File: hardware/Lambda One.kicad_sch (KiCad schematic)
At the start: 7 parts, among them IC1 01, SW1 SW_Push, U1 W65C816SxP, U2 28C256, U3 ATF22V10C, U4 AS6C1008-xxP, U5 74HC74

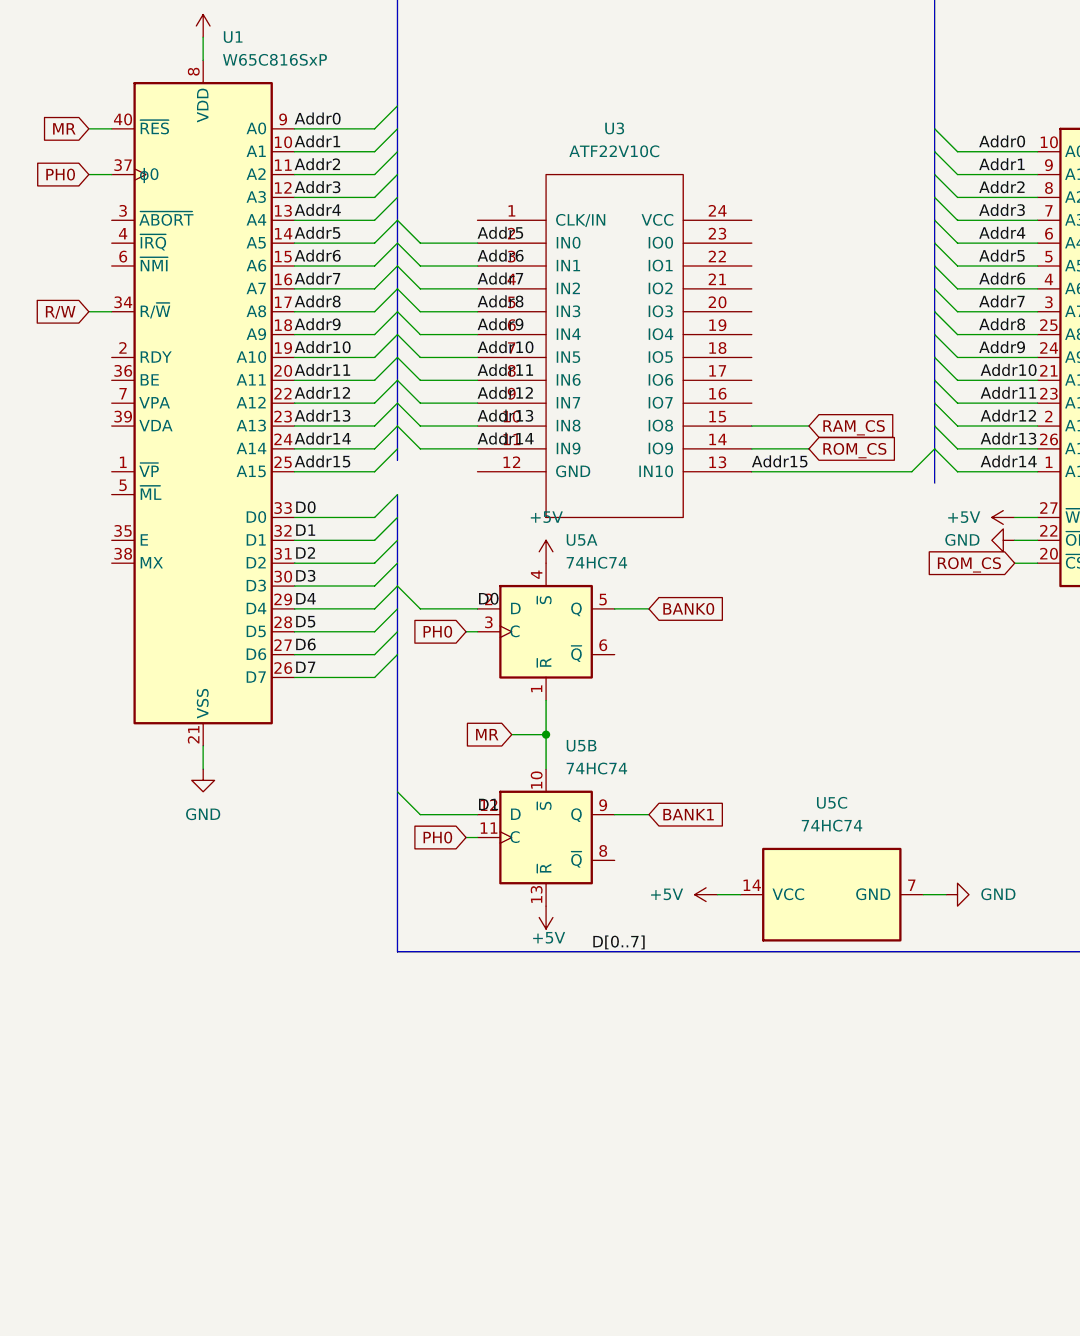
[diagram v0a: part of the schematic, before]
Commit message: Fixed mem banking
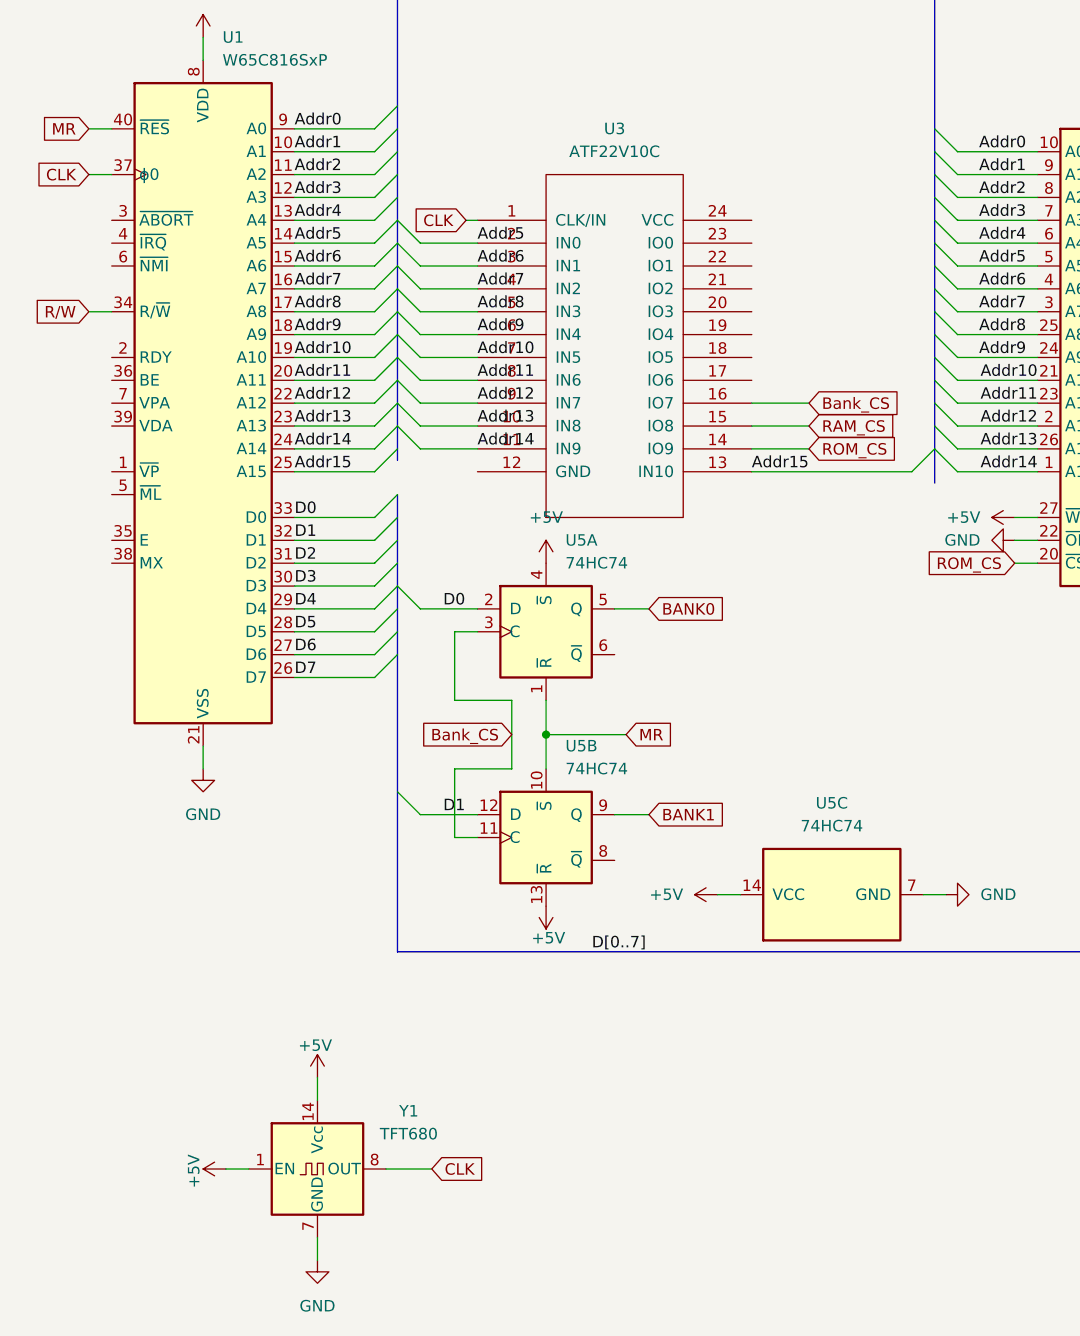
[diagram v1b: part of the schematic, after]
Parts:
- added Y1: TFT680, Oscillator:Oscillator_DIP-14, symbol Oscillator:TFT680
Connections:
- net +5V: now also Y1.1 (EN), Y1.14 (Vcc)
- net GND: now also Y1.7 (GND)
- net CLK: now reaches U3.1 (CLK/IN)
- net CLK: now also U1.37 (ϕ0), Y1.8 (OUT)
- net Bank_CS: now reaches U3.16 (IO7)
- net Bank_CS: now also U5.11 (C), U5.3 (C)
- removed net PH0: U1.37 (ϕ0), U5.11 (C), U5.3 (C)

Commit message: Modularized
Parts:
- removed U2: 28C256, symbol Memory_EEPROM:28C256
- removed U4: AS6C1008-xxP, Package_DIP:DIP-32_W15.24mm, symbol Memory_RAM:AS6C1008-xxP
- removed U5: 74HC74, symbol 74xx:74HC74
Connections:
- net GND: now also U3.12 (GND)
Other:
- added sheet Memory Sheet (mem.kicad_sch)
- moved on the sheet: IC1, SW1, U1, U3, Y1

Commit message: Added gpio
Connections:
- net GPIO_CS: now reaches U3.17 (IO6)
- net R/W renamed R/~{W}
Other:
- added sheet GPIO (gpio.kicad_sch)
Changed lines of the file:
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@@
+	(wire
+		(pts
+			(xy 175.26 87.63) (xy 181.61 87.63)
+		)
+		(stroke
+			(width 0)
+			(type default)
+		)
+	)
 	(wire
 		(pts
@@
 		)
 	)
-	(global_label "R{slash}W"
-		(shape input)
-		(at 88.9 80.01 180)
-		(fields_autoplaced yes)
-		(effects
-			(font
-				(size 1.27 1.27)
-			)
-			(justify right)
-		)
-		(property "Intersheetrefs" "${INTERSHEET_REFS}"
-			(at 81.8629 80.01 0)
-			(effects
-				(font
-					(size 1.27 1.27)
-				)
-				(justify right)
-				(hide yes)
-			)
-		)
-	)
 	(global_label "CLK"
 		(shape input)
@@
 	)
 	(global_label "ROM_CS"
-		(shape input)
+		(shape output)
 		(at 181.61 95.25 0)
 		(fields_autoplaced yes)
@@
 	)
 	(global_label "D[0..7]"
-		(shape input)
+		(shape bidirectional)
 		(at 151.13 151.13 0)
 		(fields_autoplaced yes)
@@
 		)
 		(property "Intersheetrefs" "${INTERSHEET_REFS}"
-			(at 160.7072 151.13 0)
+			(at 161.8185 151.13 0)
 			(effects
 				(font
@@
 	)
 	(global_label "Bank_CS"
-		(shape input)
+		(shape output)
 		(at 181.61 90.17 0)
 		(fields_autoplaced yes)
@@
 		)
 	)
+	(global_label "R{slash}~{W}"
+		(shape output)
+		(at 88.9 80.01 180)
+		(fields_autoplaced yes)
+		(effects
+			(font
+				(size 1.27 1.27)
+			)
+			(justify right)
+		)
+		(property "Intersheetrefs" "${INTERSHEET_REFS}"
+			(at 81.8629 80.01 0)
+			(effects
+				(font
+					(size 1.27 1.27)
+				)
+				(justify right)
+				(hide yes)
+			)
+		)
+	)
 	(global_label "Addr[0..15]"
-		(shape input)
+		(shape output)
 		(at 199.39 29.21 0)
 		(fields_autoplaced yes)
@@
 	)
 	(global_label "RAM_CS"
-		(shape input)
+		(shape output)
 		(at 181.61 92.71 0)
 		(fields_autoplaced yes)
@@
 		(property "Intersheetrefs" "${INTERSHEET_REFS}"
 			(at 191.8523 92.71 0)
+			(effects
+				(font
+					(size 1.27 1.27)
+				)
+				(justify left)
+				(hide yes)
+			)
+		)
+	)
+	(global_label "GPIO_CS"
+		(shape output)
+		(at 181.61 87.63 0)
+		(fields_autoplaced yes)
+		(effects
+			(font
+				(size 1.27 1.27)
+			)
+			(justify left)
+		)
+		(property "Intersheetrefs" "${INTERSHEET_REFS}"
+			(at 192.5176 87.63 0)
 			(effects
 				(font
@@
 				)
 			)
+		)
+	)
+	(sheet
+		(at 247.65 138.43)
+		(size 34.29 8.89)
+		(exclude_from_sim no)
+		(in_bom yes)
+		(on_board yes)
+		(dnp no)
+		(fields_autoplaced yes)
+		(stroke
+			(width 0.1524)
+			(type solid)
+		)
+		(fill
+			(color 0 0 0 0.0000)
+		)
+		(property "Sheetname" "GPIO"
+			(at 247.65 137.7184 0)
+			(effects
+				(font
+					(size 1.27 1.27)
+				)
+				(justify left bottom)
+			)
+		)
+		(property "Sheetfile" "gpio.kicad_sch"
+			(at 247.65 147.9046 0)
+			(effects
+				(font
+					(size 1.27 1.27)
+				)
+				(justify left top)
+			)
+		)
+		(instances
+			(project "Lambda One"
+				(path "/73ea9964-373f-4fdc-b03e-f532cf836c0d"
+					(page "3")
+				)
+			)

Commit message: Improved labels
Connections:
- net Bank_CS renamed BANK_{CS}
- net GPIO_CS renamed GPIO_{CS}
- net RAM_CS renamed RAM_{~{CS}}
- net ROM_CS renamed ROM_{~{CS}}
- no-connect marks 0 -> 7
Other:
- moved on the sheet: Y1
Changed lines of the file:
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@@
 		(color 0 0 0 0)
+	)
+	(no_connect
+		(at 175.26 69.85)
+	)
+	(no_connect
+		(at 175.26 72.39)
+	)
+	(no_connect
+		(at 175.26 77.47)
+	)
+	(no_connect
+		(at 175.26 82.55)
+	)
+	(no_connect
+		(at 175.26 85.09)
+	)
+	(no_connect
+		(at 175.26 80.01)
+	)
+	(no_connect
+		(at 175.26 74.93)
 	)
 	(bus_entry
@@
 	(wire
 		(pts
-			(xy 38.1 184.15) (xy 38.1 186.69)
+			(xy 246.38 55.88) (xy 246.38 58.42)
 		)
 		(stroke
@@
 	(wire
 		(pts
-			(xy 27.94 176.53) (xy 30.48 176.53)
+			(xy 236.22 48.26) (xy 238.76 48.26)
 		)
 		(stroke
@@
 	(wire
 		(pts
-			(xy 38.1 166.37) (xy 38.1 168.91)
+			(xy 246.38 38.1) (xy 246.38 40.64)
 		)
 		(stroke
@@
 	(wire
 		(pts
-			(xy 45.72 176.53) (xy 50.8 176.53)
+			(xy 254 48.26) (xy 259.08 48.26)
 		)
 		(stroke
@@
 	(global_label "CLK"
 		(shape input)
-		(at 50.8 176.53 0)
+		(at 259.08 48.26 0)
 		(fields_autoplaced yes)
 		(effects
@@
 		)
 		(property "Intersheetrefs" "${INTERSHEET_REFS}"
-			(at 57.3533 176.53 0)
+			(at 265.6333 48.26 0)
 			(effects
 				(font
@@
 		)
 	)
-	(global_label "ROM_CS"
+	(global_label "ROM_{~{CS}}"
 		(shape output)
 		(at 181.61 95.25 0)
@@
 		)
 		(property "Intersheetrefs" "${INTERSHEET_REFS}"
-			(at 192.0942 95.25 0)
+			(at 190.6815 95.25 0)
 			(effects
 				(font
@@
 		)
 	)
-	(global_label "Bank_CS"
+	(global_label "BANK_{CS}"
 		(shape output)
 		(at 181.61 90.17 0)
@@
 		)
 		(property "Intersheetrefs" "${INTERSHEET_REFS}"
-			(at 192.6384 90.17 0)
+			(at 191.5887 90.17 0)
 			(effects
 				(font
@@
 		)
 	)
-	(global_label "RAM_CS"
+	(global_label "RAM_{~{CS}}"
 		(shape output)
 		(at 181.61 92.71 0)
@@
 		)
 		(property "Intersheetrefs" "${INTERSHEET_REFS}"
-			(at 191.8523 92.71 0)
+			(at 190.4396 92.71 0)
 			(effects
 				(font
@@
 		)
 	)
-	(global_label "GPIO_CS"
+	(global_label "GPIO_{CS}"
 		(shape output)
 		(at 181.61 87.63 0)
@@
 		)
 		(property "Intersheetrefs" "${INTERSHEET_REFS}"
-			(at 192.5176 87.63 0)
+			(at 191.1049 87.63 0)
 			(effects
 				(font
@@
 	(symbol
 		(lib_id "power:+5V")
-		(at 27.94 176.53 90)
+		(at 236.22 48.26 90)
 		(unit 1)
 		(exclude_from_sim no)
@@
 		(dnp no)
 		(property "Reference" "#PWR020"
-			(at 31.75 176.53 0)
+			(at 240.03 48.26 0)
 			(effects
 				(font
@@
 		)
 		(property "Value" "+5V"
-			(at 24.384 176.784 0)
+			(at 232.664 48.514 0)
 			(effects
 				(font
@@
 		)
 		(property "Footprint" ""
-			(at 27.94 176.53 0)
+			(at 236.22 48.26 0)
 			(effects
 				(font
@@
 		)
 		(property "Datasheet" ""
-			(at 27.94 176.53 0)
+			(at 236.22 48.26 0)
 			(effects
 				(font
@@
 		)
 		(property "Description" "Power symbol creates a global label with name \"+5V\""
-			(at 27.94 176.53 0)
+			(at 236.22 48.26 0)
 			(effects
 				(font
@@
 	(symbol
 		(lib_id "power:+5V")
-		(at 38.1 166.37 0)
+		(at 246.38 38.1 0)
 		(unit 1)
 		(exclude_from_sim no)
@@
 		(dnp no)
 		(property "Reference" "#PWR014"
-			(at 38.1 170.18 0)
+			(at 246.38 41.91 0)
 			(effects
 				(font
@@
 		)
 		(property "Value" "+5V"
-			(at 38.1 162.306 0)
+			(at 246.38 34.036 0)
 			(effects
 				(font
@@
 		)
 		(property "Footprint" ""
-			(at 38.1 166.37 0)
+			(at 246.38 38.1 0)
 			(effects
 				(font
@@
 		)
 		(property "Datasheet" ""
-			(at 38.1 166.37 0)
+			(at 246.38 38.1 0)
 			(effects
 				(font
@@
 		)
 		(property "Description" "Power symbol creates a global label with name \"+5V\""
-			(at 38.1 166.37 0)
+			(at 246.38 38.1 0)
 			(effects
 				(font
@@
 	(symbol
 		(lib_id "Oscillator:TFT680")
-		(at 38.1 176.53 0)
+		(at 246.38 48.26 0)
 		(unit 1)
 		(exclude_from_sim no)
@@
 		(fields_autoplaced yes)
 		(property "Reference" "Y1"
-			(at 48.26 170.1098 0)
+			(at 256.54 41.8398 0)
 			(effects
 				(font
@@
 		)
 		(property "Value" "TFT680"
-			(at 48.26 172.6498 0)
+			(at 256.54 44.3798 0)
 			(effects
 				(font
@@
 		)
 		(property "Footprint" "Oscillator:Oscillator_DIP-14"
-			(at 49.53 185.42 0)
+			(at 257.81 57.15 0)
 			(effects
 				(font
@@
 		)
 		(property "Datasheet" "http://cdn-reichelt.de/documents/datenblatt/B400/OSZI.pdf"
-			(at 35.56 176.53 0)
+			(at 243.84 48.26 0)
 			(effects
 				(font
@@
 		)
 		(property "Description" "Crystal Clock Oscillator, DIP14-style metal package"
-			(at 38.1 176.53 0)
+			(at 246.38 48.26 0)
 			(effects
 				(font
@@
 	(symbol
 		(lib_id "power:GND")
-		(at 38.1 186.69 0)
+		(at 246.38 58.42 0)
 		(unit 1)
 		(exclude_from_sim no)
@@
 		(fields_autoplaced yes)
 		(property "Reference" "#PWR019"
-			(at 38.1 193.04 0)
+			(at 246.38 64.77 0)
 			(effects
 				(font
@@
 		)
 		(property "Value" "GND"
-			(at 38.1 191.77 0)
+			(at 246.38 63.5 0)
 			(effects
 				(font
@@
 		)
 		(property "Footprint" ""
-			(at 38.1 186.69 0)
+			(at 246.38 58.42 0)
 			(effects
 				(font
@@
 		)
 		(property "Datasheet" ""
-			(at 38.1 186.69 0)
+			(at 246.38 58.42 0)
 			(effects
 				(font
@@
 		)
 		(property "Description" "Power symbol creates a global label with name \"GND\" , ground"
-			(at 38.1 186.69 0)
-			(effects
-				(font
+			(at 246.38 58.42 0)
+			(effects
+				(font

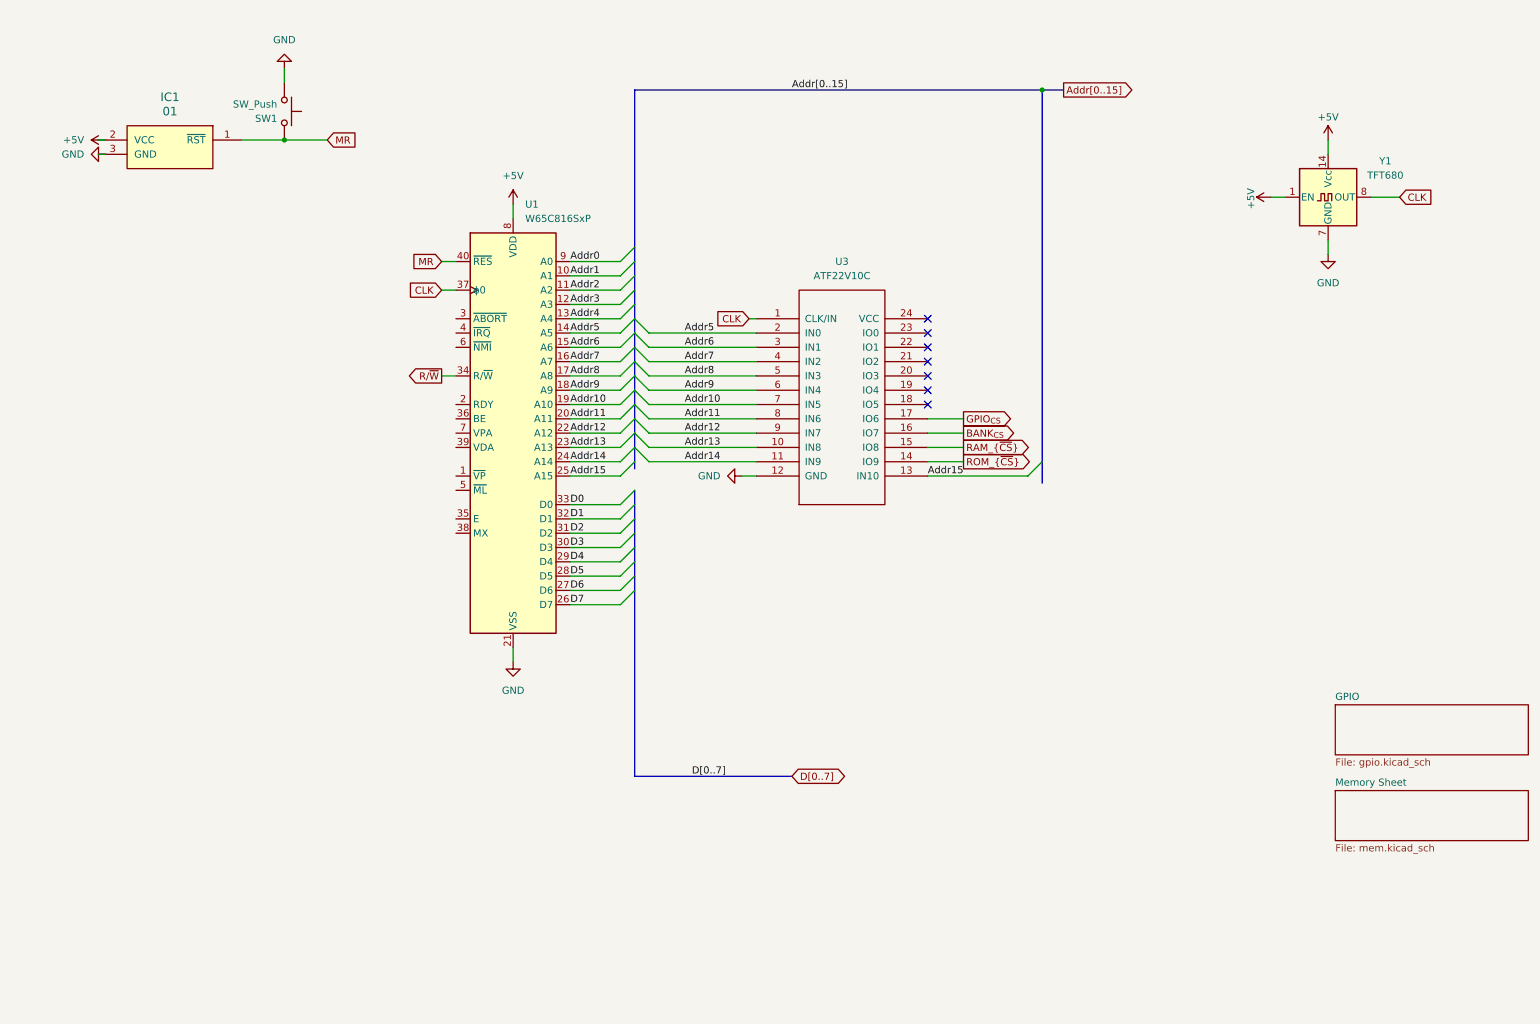
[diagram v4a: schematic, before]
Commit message: Improved Schematics and added fooprints
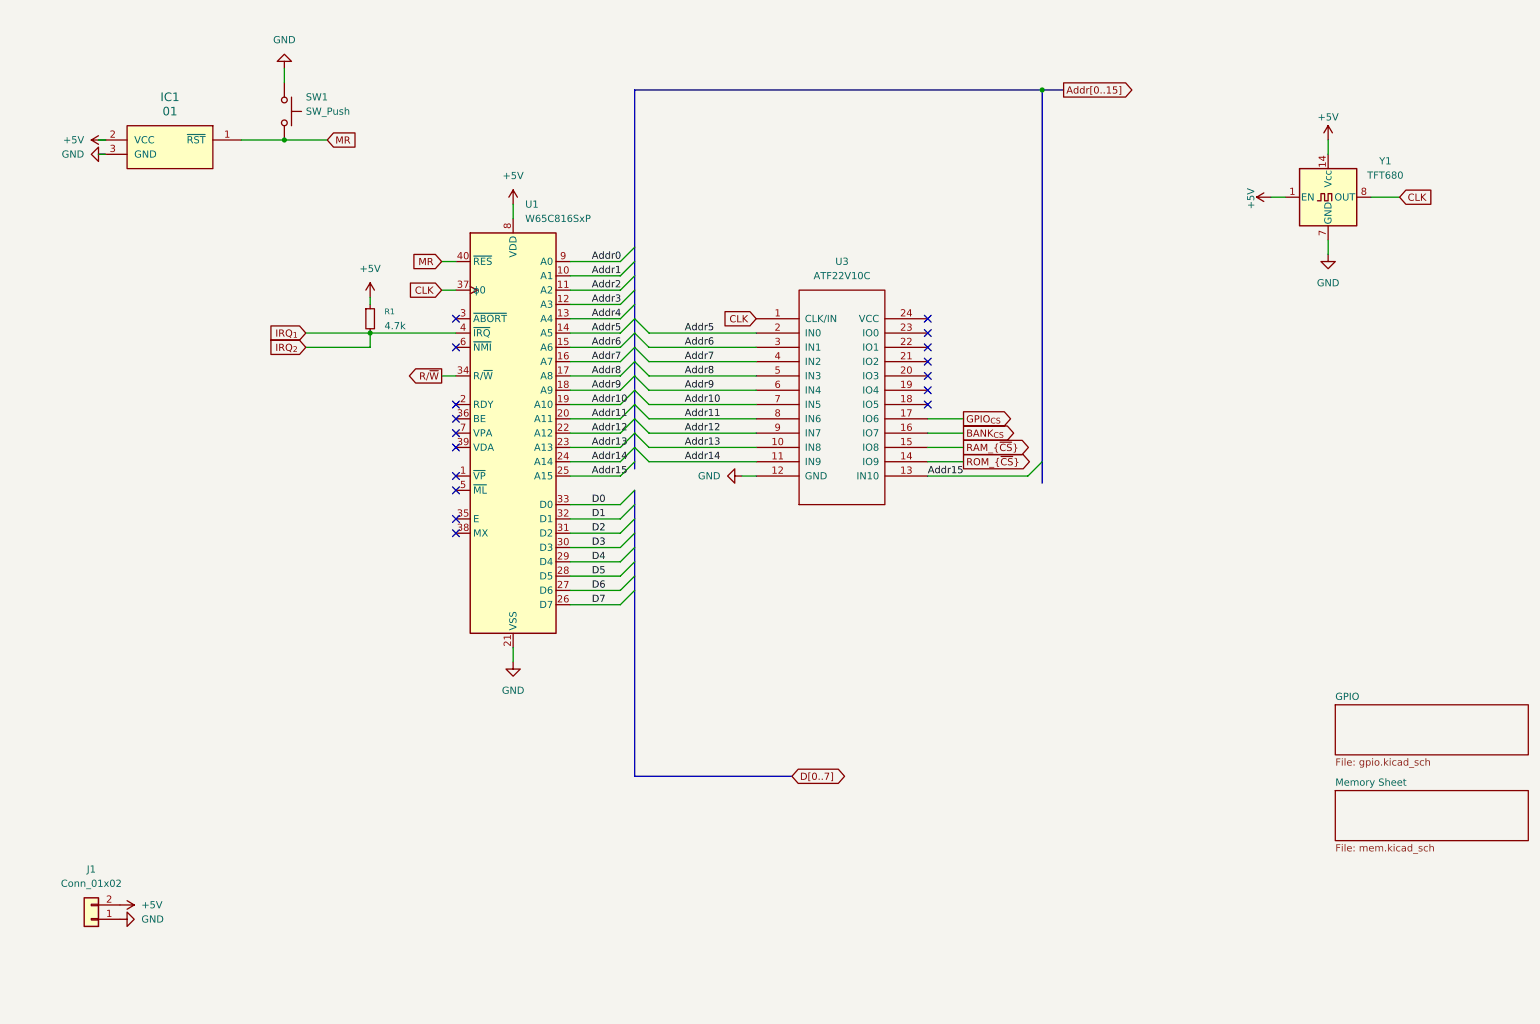
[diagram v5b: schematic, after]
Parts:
- added J1: Conn_01x02, Connector_JST:JST_XH_B2B-XH-A_1x02_P2.50mm_Vertical, symbol Connector_Generic:Conn_01x02
- added R1: 4.7k, symbol Device:R_Small
- IC1: footprint (none) -> DS1813-5:TO92127P495H695-3
- SW1: footprint (none) -> Button_Switch_SMD:SW_Push_1P1T_NO_CK_PTS125Sx73PSMTR
- U3: footprint MODULE -> ATF22V10C-10PU:24-DIP
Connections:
- net +5V: now also J1.2 (Pin_2), R1.1
- net GND: now also J1.1 (Pin_1)
- net IRQ_{1}: now reaches U1.4 (~{IRQ})
- net IRQ_{1}: now also R1.2
- no-connect marks 7 -> 17

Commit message: Added Clock and Ethernet via SPI
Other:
- added sheet Internal SPI (spi.kicad_sch)
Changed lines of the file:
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@@
 		(rev "v1")
 		(company "Embrace")
+		(comment 1 "https://github.com/Apoll011/Lambda-One")
+		(comment 2 "Apoll011")
+		(comment 3 "Draw by Tiago Inês")
 	)
 	(junction
@@
 				)
 			)
+		)
+	)
+	(sheet
+		(at 247.65 119.38)
+		(size 34.29 13.97)
+		(exclude_from_sim no)
+		(in_bom yes)
+		(on_board yes)
+		(dnp no)
+		(fields_autoplaced yes)
+		(stroke
+			(width 0.1524)
+			(type solid)
+		)
+		(fill
+			(color 0 0 0 0.0000)
+		)
+		(property "Sheetname" "Internal SPI"
+			(at 247.65 118.6684 0)
+			(effects
+				(font
+					(size 1.27 1.27)
+				)
+				(justify left bottom)
+			)
+		)
+		(property "Sheetfile" "spi.kicad_sch"
+			(at 247.65 133.9346 0)
+			(effects
+				(font
+					(size 1.27 1.27)
+				)
+				(justify left top)
+			)
+		)
+		(instances
+			(project "Lambda One"
+				(path "/73ea9964-373f-4fdc-b03e-f532cf836c0d"
+					(page "4")
+				)
+			)
